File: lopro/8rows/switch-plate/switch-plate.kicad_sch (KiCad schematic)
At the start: 89 parts

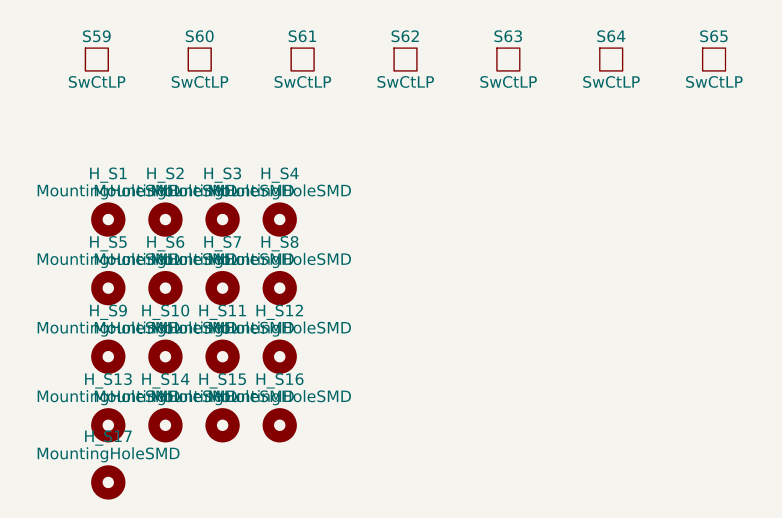
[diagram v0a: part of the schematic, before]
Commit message: add wrist support
M  giri-kicad-lib/switches.kicad_sym
A  giri-kicad-lib/switches_lib.pretty/MountingHole_1.7mm_M1.6_NoPad.kicad_mod
M  giri-kicad-lib/switches_lib.pretty/Pad_Only_SMTSO_M2.kicad_mod
A  giri-kicad-lib/switches_lib.pretty/SMTSO_M2_Hole_Only.kicad_mod
M  giri-kicad-lib/switches_lib.pretty/Switch_Cutout_LoPro.kicad_mod
A  giri-kicad-lib/switches_lib.pretty/Switch_Cutout_LoPro_R.kicad_mod
A  giri-kicad-lib/switches_lib.pretty/Switch_Cutout_LoPro_Wide.kicad_mod
M  lopro/8rows/drawborder8b.py
A  lopro/8rows/pcb/jlcpcb/gerbers/pcb-B_Cu.gbl
A  lopro/8rows/pcb/jlcpcb/gerbers/pcb-B_Mask.gbs
A  lopro/8rows/pcb/jlcpcb/gerbers/pcb-B_Paste.gbp
A  lopro/8rows/pcb/jlcpcb/gerbers/pcb-B_Silkscreen.gbo
A  lopro/8rows/pcb/jlcpcb/gerbers/pcb-Edge_Cuts.gm1
A  lopro/8rows/pcb/jlcpcb/gerbers/pcb-F_Cu.gtl
A  lopro/8rows/pcb/jlcpcb/gerbers/pcb-F_Mask.gts
A  lopro/8rows/pcb/jlcpcb/gerbers/pcb-F_Paste.gtp
A  lopro/8rows/pcb/jlcpcb/gerbers/pcb-F_Silkscreen.gto
A  lopro/8rows/pcb/jlcpcb/gerbers/pcb-NPTH-drl_map.gbr
A  lopro/8rows/pcb/jlcpcb/gerbers/pcb-NPTH.drl
A  lopro/8rows/pcb/jlcpcb/gerbers/pcb-PTH-drl_map.gbr
A  lopro/8rows/pcb/jlcpcb/gerbers/pcb-PTH.drl
M  lopro/8rows/pcb/pcb.kicad_pcb
M  lopro/8rows/placefp8b.py
M  lopro/8rows/switch-plate/fp-lib-table
M  lopro/8rows/switch-plate/switch-plate.kicad_pcb
M  lopro/8rows/switch-plate/switch-plate.kicad_prl
M  lopro/8rows/switch-plate/switch-plate.kicad_sch
M  lopro/8rows/switch-plate/sym-lib-table
A  lopro/8rows/wrist-support/fp-lib-table
A  lopro/8rows/wrist-support/sym-lib-table
A  lopro/8rows/wrist-support/wrist-support.kicad_pcb
A  lopro/8rows/wrist-support/wrist-support.kicad_prl
A  lopro/8rows/wrist-support/wrist-support.kicad_pro
A  lopro/8rows/wrist-support/wrist-support.kicad_sch
A  lopro/8rows/wrist-washer/fp-lib-table
A  lopro/8rows/wrist-washer/sym-lib-table
A  lopro/8rows/wrist-washer/wrist-washer.kicad_pcb
A  lopro/8rows/wrist-washer/wrist-washer.kicad_prl
A  lopro/8rows/wrist-washer/wrist-washer.kicad_pro
A  lop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
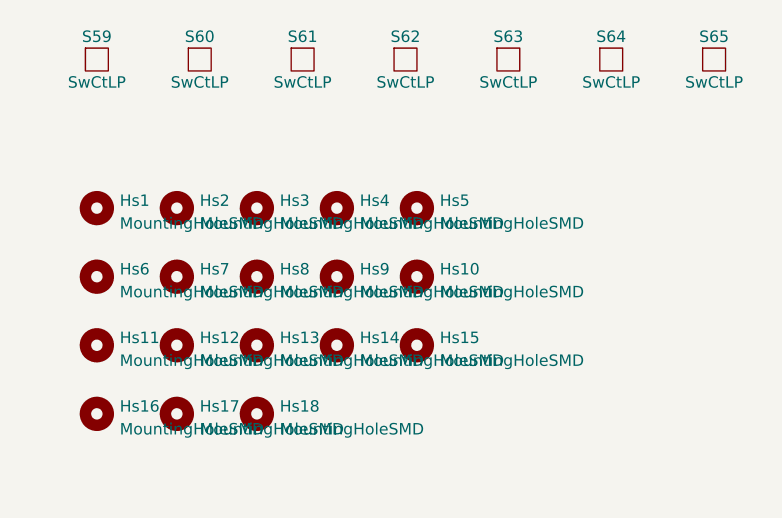
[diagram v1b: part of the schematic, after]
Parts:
- removed H_S1, H_S10, H_S11, H_S12, H_S13, H_S14, H_S15, H_S16, H_S17, H_S2, H_S3, H_S4, H_S5, H_S6, H_S7, H_S8, H_S9: MountingHoleSMD, Giri_Library:SMTSO_M2, symbol Giri:MountingHoleSMD
- added Hs1, Hs10, Hs11, Hs12, Hs13, Hs14, Hs15, Hs16, Hs17, Hs18, Hs2, Hs3, Hs4, Hs5, Hs6, Hs7, Hs8, Hs9: MountingHoleSMD, Giri_Library:MountingHole_1.7mm_M1.6_Pad, symbol Giri:MountingHoleSMD

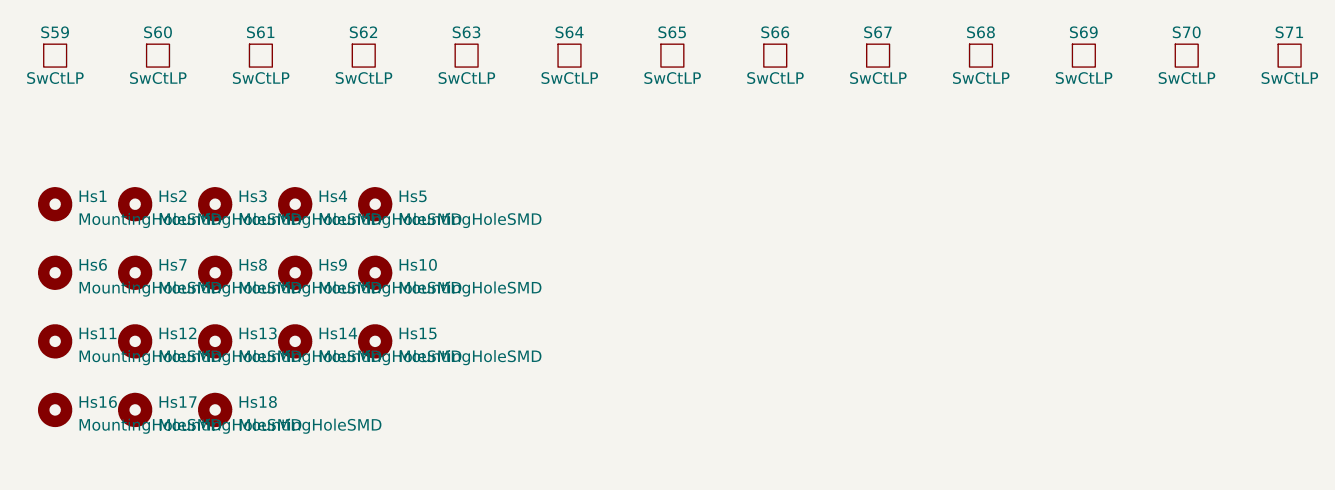
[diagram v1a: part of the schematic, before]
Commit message: enlarge center hole of keychron switch footprint
M  giri-kicad-lib/switches.kicad_sym
M  giri-kicad-lib/switches_lib.pretty/Keychron_Optical_Switch_1u.kicad_mod
M  giri-kicad-lib/switches_lib.pretty/Keychron_Optical_Switch_R_1u.kicad_mod
A  giri-kicad-lib/switches_lib.pretty/USB_C_Receptacle_Outline_XKB_U262-16XN-4BVC11.kicad_mod
M  lopro/8rows/border8r.py
D  lopro/8rows/pcb/jlcpcb/gerbers/pcb-B_Cu.gbl
D  lopro/8rows/pcb/jlcpcb/gerbers/pcb-F_Cu.gtl
D  lopro/8rows/pcb/jlcpcb/gerbers/pcb-F_Paste.gtp
D  lopro/8rows/pcb/jlcpcb/gerbers/pcb-F_Silkscreen.gto
D  lopro/8rows/pcb/jlcpcb/gerbers/pcb-NPTH-drl_map.gbr
D  lopro/8rows/pcb/jlcpcb/gerbers/pcb-PTH-drl_map.gbr
D  lopro/8rows/pcb/jlcpcb/gerbers/pcb-PTH.drl
A  lopro/8rows/pcb/jlcpcb/gerbers1p2/pcb-B_Cu.gbl
R  lopro/8rows/pcb/jlcpcb/gerbers/pcb-B_Mask.gbs -> lopro/8rows/pcb/jlcpcb/gerbers1p2/pcb-B_Mask.gbs
R  lopro/8rows/pcb/jlcpcb/gerbers/pcb-B_Paste.gbp -> lopro/8rows/pcb/jlcpcb/gerbers1p2/pcb-B_Paste.gbp
R  lopro/8rows/pcb/jlcpcb/gerbers/pcb-B_Silkscreen.gbo -> lopro/8rows/pcb/jlcpcb/gerbers1p2/pcb-B_Silkscreen.gbo
R  lopro/8rows/pcb/jlcpcb/gerbers/pcb-Edge_Cuts.gm1 -> lopro/8rows/pcb/jlcpcb/gerbers1p2/pcb-Edge_Cuts.gm1
A  lopro/8rows/pcb/jlcpcb/gerbers1p2/pcb-F_Cu.gtl
R  lopro/8rows/pcb/jlcpcb/gerbers/pcb-F_Mask.gts -> lopro/8rows/pcb/jlcpcb/gerbers1p2/pcb-F_Mask.gts
A  lopro/8rows/pcb/jlcpcb/gerbers1p2/pcb-F_Paste.gtp
A  lopro/8rows/pcb/jlcpcb/gerbers1p2/pcb-F_Silkscreen.gto
A  lopro/8rows/pcb/jlcpcb/gerbers1p2/pcb-NPTH-drl_map.gbr
R  lopro/8rows/pcb/jlcpcb/gerbers/pcb-NPTH.drl -> lopro/8rows/pcb/jlcpcb/gerbers1p2/pcb-NPTH.drl
A  lopro/8rows/pcb/jlcpcb/gerbers1p2/pcb-PTH-drl_map.gbr
A  lopro/8rows/pcb/jlcpcb/gerbers1p2/pcb-PTH.drl
A  lopro/8rows/pcb/pcb-b.jpg
D  lopro/8rows/pcb/pcb-b.png
D  lopro/8rows/pcb/pcb-f.png
A  lopro/8rows/pcb/pcb.jpg
M  lopro/8rows/pcb/pcb.kicad_pcb
M  lopro/8rows/pcb/pcb.kicad_prl
M  lopro/8rows/pcb/pcb.kicad_pro
M  lopro/8rows/pickle8r.py
M  lopro/8rows/place8r.py
A  lopro/8rows/switch-pl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
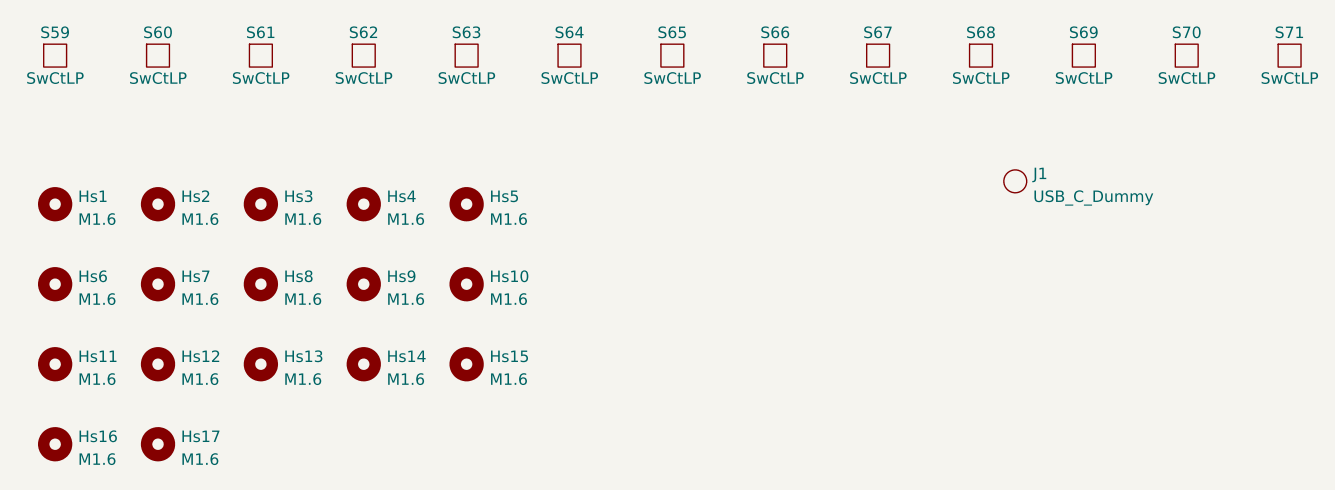
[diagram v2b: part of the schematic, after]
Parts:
- removed Hs18: MountingHoleSMD, Giri_Library:MountingHole_1.7mm_M1.6_Pad, symbol Giri:MountingHoleSMD
- added J1: USB_C_Dummy, Giri_Library:USB_C_Receptacle_Outline_XKB_U262-16XN-4BVC11, symbol Giri:USB_C_Dummy
- Hs1, Hs10, Hs11, Hs12, Hs13, Hs14, Hs15, Hs16, Hs17, Hs2, Hs3, Hs4, Hs5, Hs6, Hs7, Hs8, Hs9: value MountingHoleSMD -> M1.6; footprint Giri_Library:MountingHole_1.7mm_M1.6_Pad -> Giri_Library:MountingHole_1.7mm_M1.6_NoPad
